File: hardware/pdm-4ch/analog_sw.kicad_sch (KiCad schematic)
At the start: 41 parts, among them J5 Conn_02x05_Top_Bottom, Q3 BC817-40, Q4 BC817-40, Q5 BC817-40, Q6 BC817-40

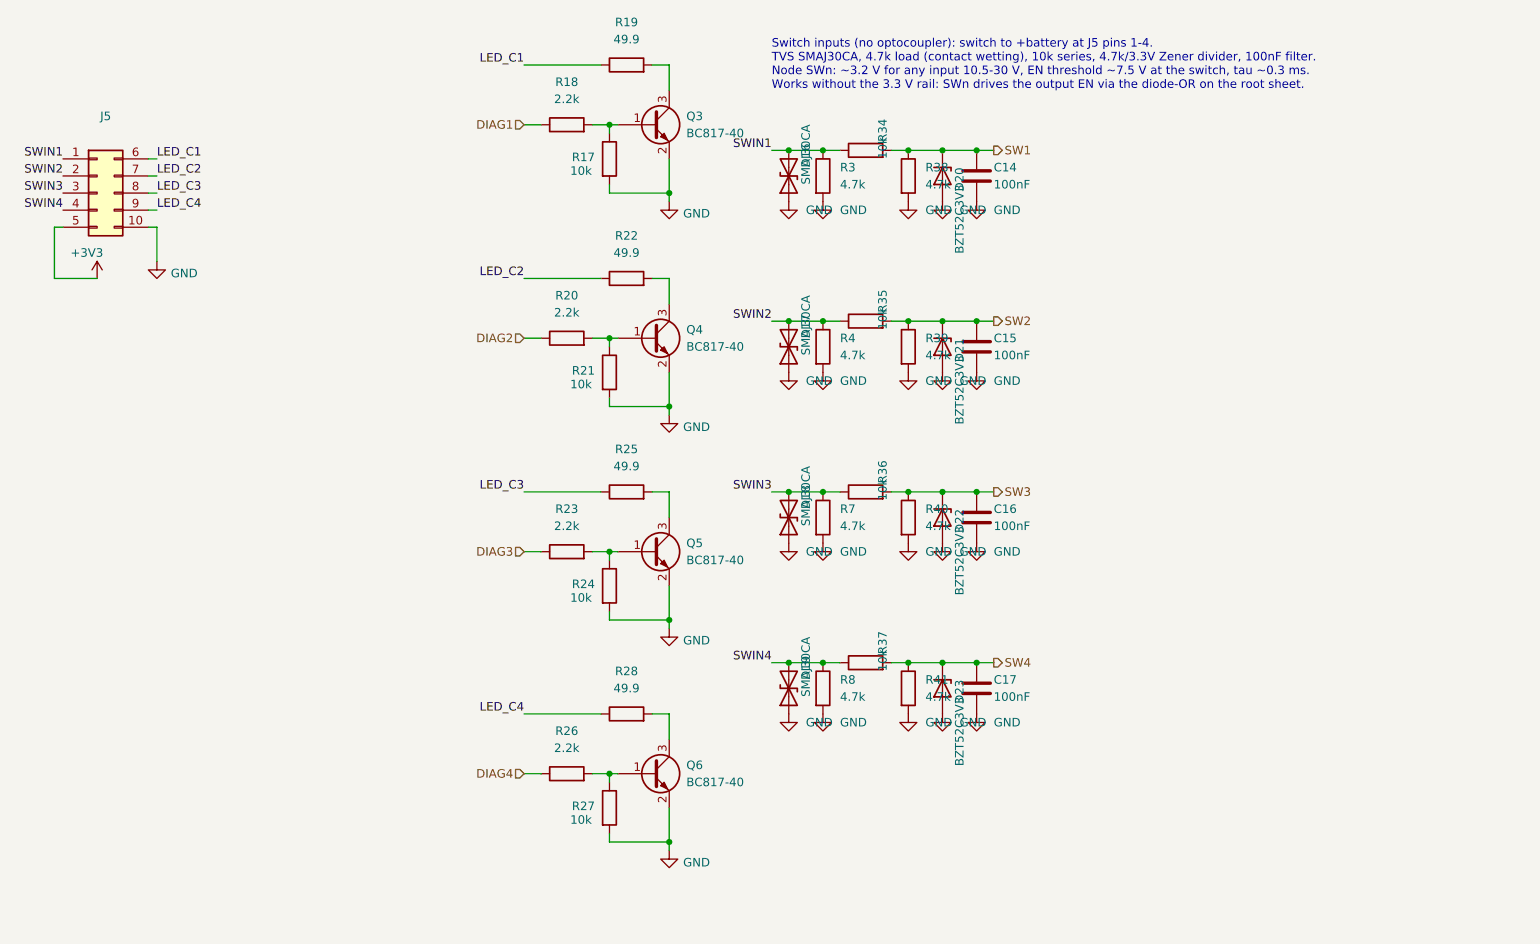
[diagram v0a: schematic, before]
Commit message: System: panel cable and pin map – fused switch supply, MMBT5551 LED sinks, VBAT and NTC (decisions 17-21)
Co-Authored-By: Claude Opus 5.5 <noreply@anthropic.com>
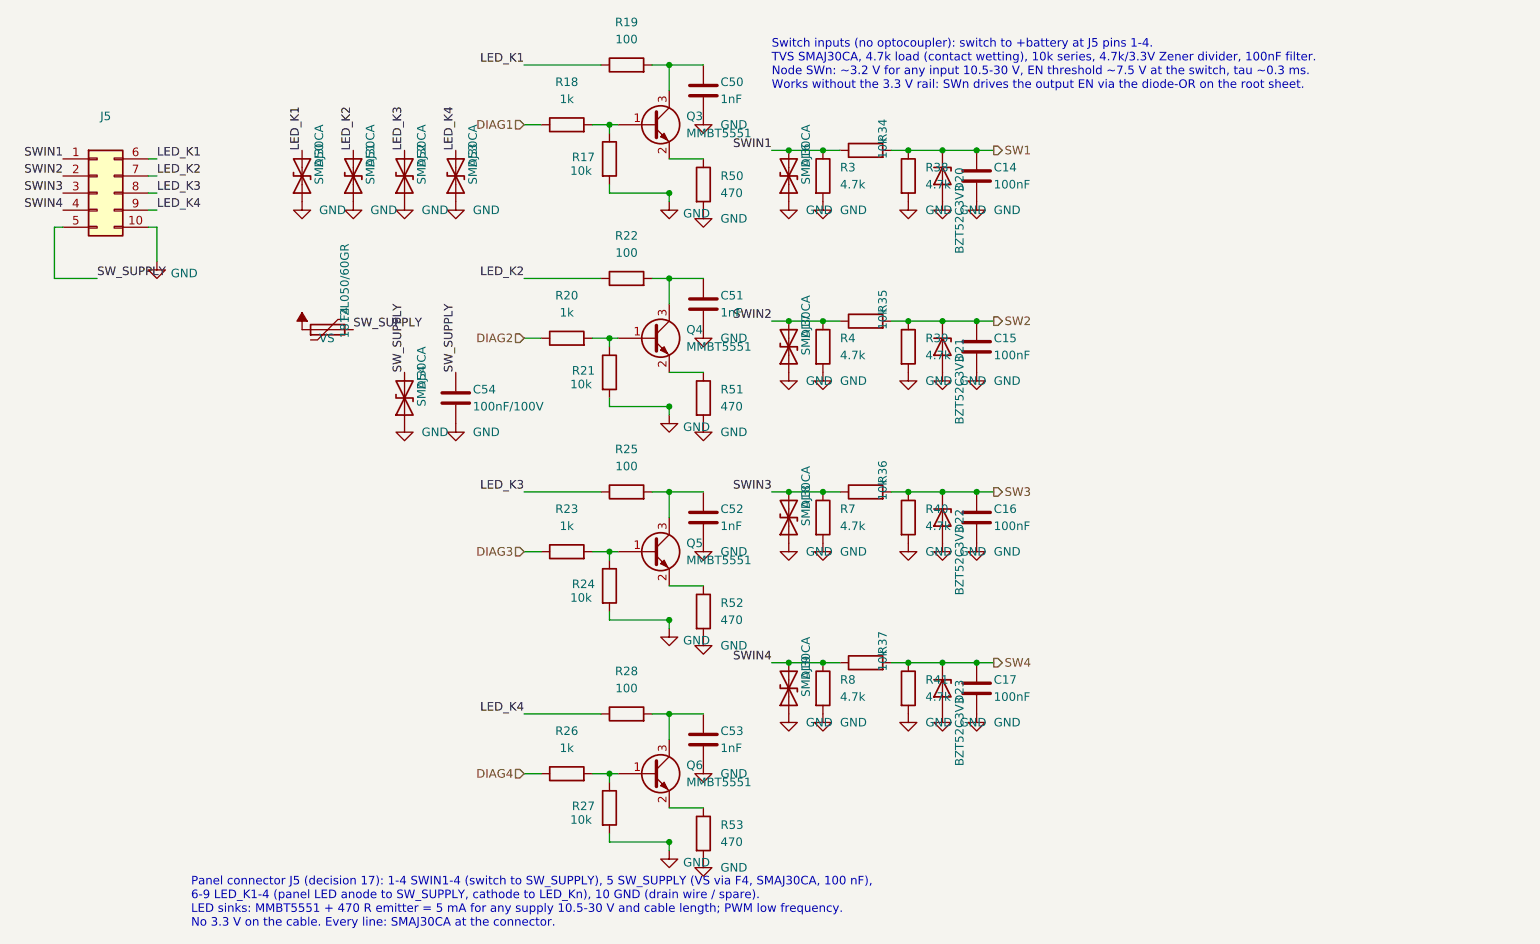
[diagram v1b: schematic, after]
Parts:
- added C50, C51, C52, C53: 1nF, Capacitor_SMD:C_0402_1005Metric, symbol Device:C
- added C54: 100nF/100V, Capacitor_SMD:C_0805_2012Metric, symbol Device:C
- added D50, D51, D52, D53, D54: SMAJ30CA, Diode_SMD:D_SMA, symbol Device:D_TVS
- added F4: 1812L050/60GR, Fuse:Fuse_1812_4532Metric, symbol Device:Polyfuse
- added R50, R51, R52, R53: 470, Resistor_SMD:R_0402_1005Metric, symbol Device:R
- Q3, Q4, Q5, Q6: value BC817-40 -> MMBT5551; LCSC C20069155 -> C2145
- R18, R20, R23, R26: value 2.2k -> 1k; LCSC (none) -> C11702
- R19, R22, R25, R28: value 49.9 -> 100; LCSC C25120 -> C25076
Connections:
- net GND: now also C50.2, C51.2, C52.2, C53.2, C54.2, D50.1 (A1), D51.1 (A1), D52.1 (A1), D53.1 (A1), D54.1 (A1), R50.2, R51.2, R52.2, R53.2; no longer Q3.2 (E), Q4.2 (E), Q5.2 (E), Q6.2 (E)
- net at Q4.3 (C), R22.2: now also C51.1
- net at Q5.3 (C), R25.2: now also C52.1
- net at Q3.3 (C), R19.2: now also C50.1
- net at Q6.3 (C), R28.2: now also C53.1
- net +3V3 renamed SW_SUPPLY
- net SW_SUPPLY: now also C54.1, D54.2 (A2), F4.2
- net LED_C1 renamed LED_K1
- net LED_K1: now also D50.2 (A2)
- net LED_C2 renamed LED_K2
- net LED_K2: now also D51.2 (A2)
- net LED_C3 renamed LED_K3
- net LED_K3: now also D52.2 (A2)
- net LED_C4 renamed LED_K4
- net LED_K4: now also D53.2 (A2)
- new net: Q4.2 (E), R51.1
- new net: Q6.2 (E), R53.1
- new net: Q5.2 (E), R52.1
- new net: Q3.2 (E), R50.1
- new net VS: F4.1
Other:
- note added: "Panel connector J5 (decision 17): 1-4 SWIN1-4 (switch to SW_SUPPLY), 5 SW_SUPPLY (VS via F4, SMAJ30CA, 100 nF), 6-9 LED_K1-4 (panel LED anode to SW_SUPPLY, cathode to LED_Kn), 10 GND (drain wire / spare). LED sinks: MMBT5551 + 470 R emitter = 5 mA for any supply 10.5-30 V and cable length; PWM low frequency. No 3.3 V on the cable. Every line: SMAJ30CA at the connector."
